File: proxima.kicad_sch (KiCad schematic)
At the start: 11 parts

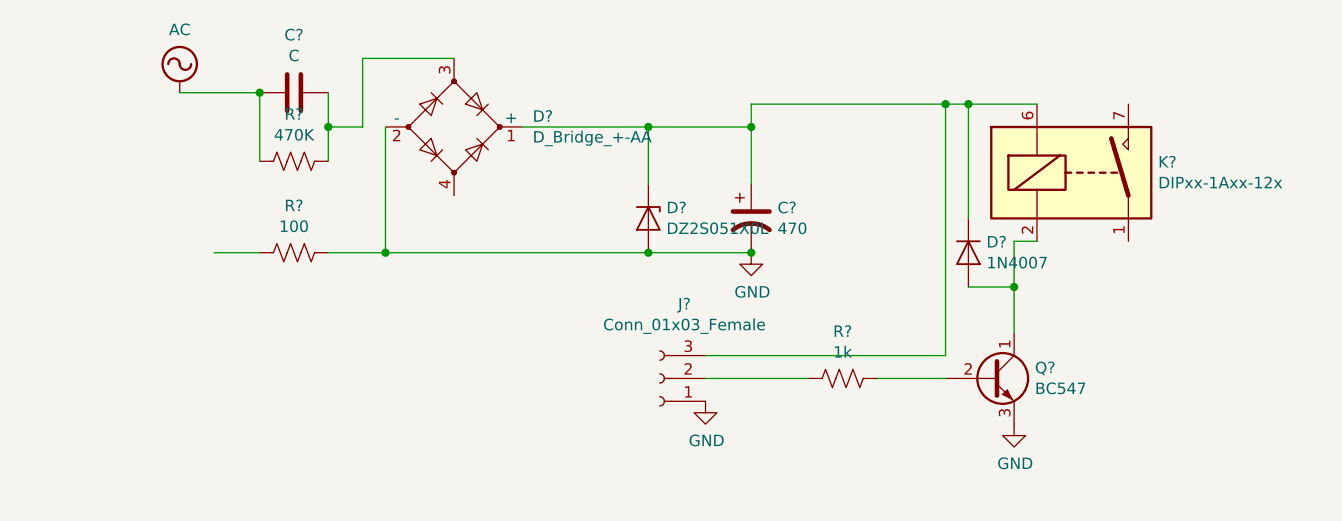
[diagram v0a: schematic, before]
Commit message: Annotate symbols
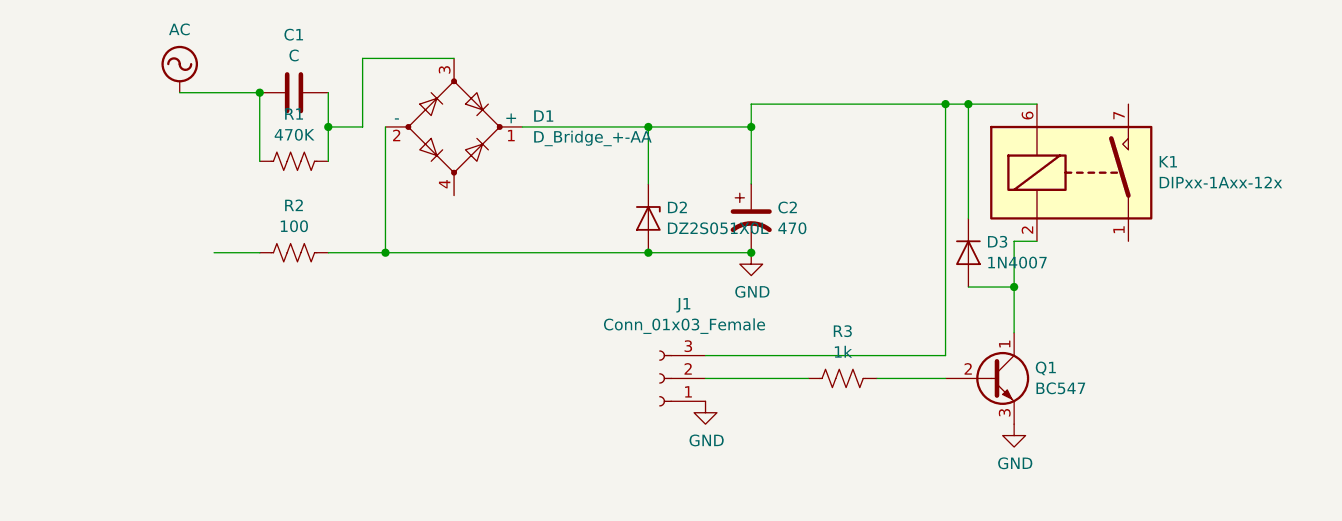
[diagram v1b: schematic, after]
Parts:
- gave numbers to parts that had none: 11
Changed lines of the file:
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@@
   (symbol (lib_id "proxima-rescue:C-Device") (at 124.46 77.47 270) (unit 1)
     (in_bom yes) (on_board yes)
-    (property "Reference" "C?" (id 0) (at 124.46 71.0692 90))
+    (property "Reference" "C1" (id 0) (at 124.46 71.0692 90))
     (property "Value" "C" (id 1) (at 124.46 73.3806 90))
     (property "Footprint" "" (id 2) (at 120.65 78.4352 0)
@@
   (symbol (lib_id "proxima-rescue:CP1-Device") (at 175.26 91.44 0) (unit 1)
     (in_bom yes) (on_board yes)
-    (property "Reference" "C?" (id 0) (at 178.181 90.2716 0)
+    (property "Reference" "C2" (id 0) (at 178.181 90.2716 0)
       (effects (font (size 1.27 1.27)) (justify left))
     )
@@
   (symbol (lib_id "proxima-rescue:D_Bridge_+-AA-Device") (at 142.24 81.28 0) (unit 1)
     (in_bom yes) (on_board yes)
-    (property "Reference" "D?" (id 0) (at 150.9776 80.1116 0)
+    (property "Reference" "D1" (id 0) (at 150.9776 80.1116 0)
       (effects (font (size 1.27 1.27)) (justify left))
     )
@@
   (symbol (lib_id "proxima-rescue:DZ2S051X0L-Diode") (at 163.83 91.44 270) (unit 1)
     (in_bom yes) (on_board yes)
-    (property "Reference" "D?" (id 0) (at 165.8366 90.2716 90)
+    (property "Reference" "D2" (id 0) (at 165.8366 90.2716 90)
       (effects (font (size 1.27 1.27)) (justify left))
     )
@@
   (symbol (lib_id "proxima-rescue:R_US-Device") (at 124.46 85.09 270) (unit 1)
     (in_bom yes) (on_board yes)
-    (property "Reference" "R?" (id 0) (at 124.46 79.883 90))
+    (property "Reference" "R1" (id 0) (at 124.46 79.883 90))
     (property "Value" "470K" (id 1) (at 124.46 82.1944 90))
     (property "Footprint" "" (id 2) (at 124.206 86.106 90)
@@
   (symbol (lib_id "proxima-rescue:R_US-Device") (at 124.46 95.25 270) (unit 1)
     (in_bom yes) (on_board yes)
-    (property "Reference" "R?" (id 0) (at 124.46 90.043 90))
+    (property "Reference" "R2" (id 0) (at 124.46 90.043 90))
     (property "Value" "100" (id 1) (at 124.46 92.3544 90))
     (property "Footprint" "" (id 2) (at 124.206 96.266 90)
@@
   (symbol (lib_id "proxima-rescue:AC-power") (at 111.76 77.47 0) (unit 1)
     (in_bom yes) (on_board yes)
-    (property "Reference" "#PWR?" (id 0) (at 111.76 80.01 0)
+    (property "Reference" "#PWR01" (id 0) (at 111.76 80.01 0)
       (effects (font (size 1.27 1.27)) hide)
     )
@@
   (symbol (lib_id "proxima-rescue:DIPxx-1Axx-12x-Relay") (at 212.09 86.36 0) (unit 1)
     (in_bom yes) (on_board yes)
-    (property "Reference" "K?" (id 0) (at 220.472 85.1916 0)
+    (property "Reference" "K1" (id 0) (at 220.472 85.1916 0)
       (effects (font (size 1.27 1.27)) (justify left))
     )
@@
   (symbol (lib_id "proxima-rescue:BC547-Transistor_BJT") (at 201.93 109.22 0) (unit 1)
     (in_bom yes) (on_board yes)
-    (property "Reference" "Q?" (id 0) (at 206.7814 108.0516 0)
+    (property "Reference" "Q1" (id 0) (at 206.7814 108.0516 0)
       (effects (font (size 1.27 1.27)) (justify left))
     )
@@
   (symbol (lib_id "proxima-rescue:Conn_01x03_Female-Connector") (at 165.1 109.22 180) (unit 1)
     (in_bom yes) (on_board yes)
-    (property "Reference" "J?" (id 0) (at 167.8432 100.965 0))
+    (property "Reference" "J1" (id 0) (at 167.8432 100.965 0))
     (property "Value" "Conn_01x03_Female" (id 1) (at 167.8432 103.2764 0))
     (property "Footprint" "" (id 2) (at 165.1 109.22 0)
@@
   (symbol (lib_id "proxima-rescue:R_US-Device") (at 185.42 109.22 270) (unit 1)
     (in_bom yes) (on_board yes)
-    (property "Reference" "R?" (id 0) (at 185.42 104.013 90))
+    (property "Reference" "R3" (id 0) (at 185.42 104.013 90))
     (property "Value" "1k" (id 1) (at 185.42 106.3244 90))
     (property "Footprint" "" (id 2) (at 185.166 110.236 90)
@@
   (symbol (lib_id "proxima-rescue:GND-power") (at 175.26 95.25 0) (unit 1)
     (in_bom yes) (on_board yes)
-    (property "Reference" "#PWR?" (id 0) (at 175.26 101.6 0)
+    (property "Reference" "#PWR03" (id 0) (at 175.26 101.6 0)
       (effects (font (size 1.27 1.27)) hide)
     )
@@
   (symbol (lib_id "proxima-rescue:GND-power") (at 204.47 114.3 0) (unit 1)
     (in_bom yes) (on_board yes)
-    (property "Reference" "#PWR?" (id 0) (at 204.47 120.65 0)
+    (property "Reference" "#PWR04" (id 0) (at 204.47 120.65 0)
       (effects (font (size 1.27 1.27)) hide)
     )
@@
   (symbol (lib_id "proxima-rescue:GND-power") (at 170.18 111.76 0) (unit 1)
     (in_bom yes) (on_board yes)
-    (property "Reference" "#PWR?" (id 0) (at 170.18 118.11 0)
+    (property "Reference" "#PWR02" (id 0) (at 170.18 118.11 0)
       (effects (font (size 1.27 1.27)) hide)
     )
@@
   (symbol (lib_id "proxima-rescue:1N4007-Diode") (at 199.39 95.25 270) (unit 1)
     (in_bom yes) (on_board yes)
-    (property "Reference" "D?" (id 0) (at 201.3966 94.0816 90)
+    (property "Reference" "D3" (id 0) (at 201.3966 94.0816 90)
       (effects (font (size 1.27 1.27)) (justify left))
     )
@@
   (symbol_instances
     (path "/00000000-0000-0000-0000-00006363069b"
-      (reference "#PWR?") (unit 1) (value "AC") (footprint "")
+      (reference "#PWR01") (unit 1) (value "AC") (footprint "")
+    )
+    (path "/00000000-0000-0000-0000-0000636b6e73"
+      (reference "#PWR02") (unit 1) (value "GND") (footprint "")
     )
     (path "/00000000-0000-0000-0000-0000636b5108"
-      (reference "#PWR?") (unit 1) (value "GND") (footprint "")
+      (reference "#PWR03") (unit 1) (value "GND") (footprint "")
     )
     (path "/00000000-0000-0000-0000-0000636b5b8d"
-      (reference "#PWR?") (unit 1) (value "GND") (footprint "")
-    )
-    (path "/00000000-0000-0000-0000-0000636b6e73"
-      (reference "#PWR?") (unit 1) (value "GND") (footprint "")
+      (reference "#PWR04") (unit 1) (value "GND") (footprint "")
     )
     (path "/00000000-0000-0000-0000-00006362c072"
-      (reference "C?") (unit 1) (value "C") (footprint "")
+      (reference "C1") (unit 1) (value "C") (footprint "")
     )
     (path "/00000000-0000-0000-0000-00006362c51f"
-      (reference "C?") (unit 1) (value "470") (footprint "")
+      (reference "C2") (unit 1) (value "470") (footprint "")
     )
     (path "/00000000-0000-0000-0000-00006362d2c4"
-      (reference "D?") (unit 1) (value "D_Bridge_+-AA") (footprint "")
+      (reference "D1") (unit 1) (value "D_Bridge_+-AA") (footprint "")
     )
     (path "/00000000-0000-0000-0000-00006362e947"
-      (reference "D?") (unit 1) (value "DZ2S051X0L") (footprint "Diode_SMD:D_SOD-523")
+      (reference "D2") (unit 1) (value "DZ2S051X0L") (footprint "Diode_SMD:D_SOD-523")
     )
     (path "/00000000-0000-0000-0000-0000636b8955"
-      (reference "D?") (unit 1) (value "1N4007") (footprint "Diode_THT:D_DO-41_SOD81_P10.16mm_Horizontal")
+      (reference "D3") (unit 1) (value "1N4007") (footprint "Diode_THT:D_DO-41_SOD81_P10.16mm_Horizontal")
     )
     (path "/00000000-0000-0000-0000-0000636a603e"
-      (reference "J?") (unit 1) (value "Conn_01x03_Female") (footprint "")
+      (reference "J1") (unit 1) (value "Conn_01x03_Female") (footprint "")
     )
     (path "/00000000-0000-0000-0000-000063693c13"
-      (reference "K?") (unit 1) (value "DIPxx-1Axx-12x") (footprint "Relay_THT:Relay_StandexMeder_DIP_LowProfile")
+      (reference "K1") (unit 1) (value "DIPxx-1Axx-12x") (footprint "Relay_THT:Relay_StandexMeder_DIP_LowProfile")
     )
     (path "/00000000-0000-0000-0000-000063695ded"
-      (reference "Q?") (unit 1) (value "BC547") (footprint "Package_TO_SOT_THT:TO-92_Inline")
+      (reference "Q1") (unit 1) (value "BC547") (footprint "Package_TO_SOT_THT:TO-92_Inline")
     )
     (path "/00000000-0000-0000-0000-00006362f5cb"
-      (reference "R?") (unit 1) (value "470K") (footprint "")
+      (reference "R1") (unit 1) (value "470K") (footprint "")
     )
     (path "/00000000-0000-0000-0000-000063630132"
-      (reference "R?") (unit 1) (value "100") (footprint "")
+      (reference "R2") (unit 1) (value "100") (footprint "")
     )
     (path "/00000000-0000-0000-0000-0000636acf39"
-      (reference "R?") (unit 1) (value "1k") (footprint "")
-    )
-  )
+      (reference "R3") (unit 1) (value "1k") (footprint "")
+    )
+  )

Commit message: Substitute proxima-rescue lib
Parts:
- C1: symbol proxima-rescue:C-Device -> Device:C
- C2: symbol proxima-rescue:CP1-Device -> Device:C_Polarized_US
- D1: symbol proxima-rescue:D_Bridge_+-AA-Device -> Device:D_Bridge_+AA-
- D2: symbol proxima-rescue:DZ2S051X0L-Diode -> Diode:DZ2S051X0L
- D3: symbol proxima-rescue:1N4007-Diode -> Diode:1N4007
- J1: symbol proxima-rescue:Conn_01x03_Female-Connector -> Connector:Conn_01x03_Female
- K1: symbol proxima-rescue:DIPxx-1Axx-12x-Relay -> Relay:DIPxx-1Axx-12x
- Q1: symbol proxima-rescue:BC547-Transistor_BJT -> Transistor_BJT:BC547
- R1, R2, R3: symbol proxima-rescue:R_US-Device -> Device:R_US
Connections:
- net GND: now also D1.4 (-); no longer D1.2 (-)
- net at C1.1, R1.1: now also D1.2; no longer D1.3
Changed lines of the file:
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@@
     (stroke (width 0) (type default) (color 0 0 0 0))
   )
-  (symbol (lib_id "proxima-rescue:C-Device") (at 124.46 77.47 270) (unit 1)
+  (symbol (lib_id "Device:C") (at 124.46 77.47 270) (unit 1)
     (in_bom yes) (on_board yes)
     (property "Reference" "C1" (id 0) (at 124.46 71.0692 90))
@@
     (pin "2")
   )
-  (symbol (lib_id "proxima-rescue:CP1-Device") (at 175.26 91.44 0) (unit 1)
+  (symbol (lib_id "Device:C_Polarized_US") (at 175.26 91.44 0) (unit 1)
     (in_bom yes) (on_board yes)
     (property "Reference" "C2" (id 0) (at 178.181 90.2716 0)
@@
     (pin "2")
   )
-  (symbol (lib_id "proxima-rescue:D_Bridge_+-AA-Device") (at 142.24 81.28 0) (unit 1)
+  (symbol (lib_id "Device:D_Bridge_+AA-") (at 142.24 81.28 0) (unit 1)
     (in_bom yes) (on_board yes)
     (property "Reference" "D1" (id 0) (at 150.9776 80.1116 0)
@@
     (pin "4")
   )
-  (symbol (lib_id "proxima-rescue:DZ2S051X0L-Diode") (at 163.83 91.44 270) (unit 1)
+  (symbol (lib_id "Diode:DZ2S051X0L") (at 163.83 91.44 270) (unit 1)
     (in_bom yes) (on_board yes)
     (property "Reference" "D2" (id 0) (at 165.8366 90.2716 90)
@@
     (pin "2")
   )
-  (symbol (lib_id "proxima-rescue:R_US-Device") (at 124.46 85.09 270) (unit 1)
+  (symbol (lib_id "Device:R_US") (at 124.46 85.09 270) (unit 1)
     (in_bom yes) (on_board yes)
     (property "Reference" "R1" (id 0) (at 124.46 79.883 90))
@@
     (pin "2")
   )
-  (symbol (lib_id "proxima-rescue:R_US-Device") (at 124.46 95.25 270) (unit 1)
+  (symbol (lib_id "Device:R_US") (at 124.46 95.25 270) (unit 1)
     (in_bom yes) (on_board yes)
     (property "Reference" "R2" (id 0) (at 124.46 90.043 90))
@@
     (pin "2")
   )
-  (symbol (lib_id "proxima-rescue:AC-power") (at 111.76 77.47 0) (unit 1)
+  (symbol (lib_id "power:AC") (at 111.76 77.47 0) (unit 1)
     (in_bom yes) (on_board yes)
     (property "Reference" "#PWR01" (id 0) (at 111.76 80.01 0)
@@
     (pin "1")
   )
-  (symbol (lib_id "proxima-rescue:DIPxx-1Axx-12x-Relay") (at 212.09 86.36 0) (unit 1)
+  (symbol (lib_id "Relay:DIPxx-1Axx-12x") (at 212.09 86.36 0) (unit 1)
     (in_bom yes) (on_board yes)
     (property "Reference" "K1" (id 0) (at 220.472 85.1916 0)
@@
     (pin "8")
   )
-  (symbol (lib_id "proxima-rescue:BC547-Transistor_BJT") (at 201.93 109.22 0) (unit 1)
+  (symbol (lib_id "Transistor_BJT:BC547") (at 201.93 109.22 0) (unit 1)
     (in_bom yes) (on_board yes)
     (property "Reference" "Q1" (id 0) (at 206.7814 108.0516 0)
@@
       (effects (font (size 1.27 1.27) italic) (justify left) hide)
     )
-    (property "Datasheet" "http://www.fairchildsemi.com/ds/BC/BC547.pdf" (id 3) (at 201.93 109.22 0)
+    (property "Datasheet" "https://www.onsemi.com/pub/Collateral/BC550-D.pdf" (id 3) (at 201.93 109.22 0)
       (effects (font (size 1.27 1.27)) (justify left) hide)
     )
@@
     (pin "3")
   )
-  (symbol (lib_id "proxima-rescue:Conn_01x03_Female-Connector") (at 165.1 109.22 180) (unit 1)
+  (symbol (lib_id "Connector:Conn_01x03_Female") (at 165.1 109.22 180) (unit 1)
     (in_bom yes) (on_board yes)
     (property "Reference" "J1" (id 0) (at 167.8432 100.965 0))
@@
     (pin "3")
   )
-  (symbol (lib_id "proxima-rescue:R_US-Device") (at 185.42 109.22 270) (unit 1)
+  (symbol (lib_id "Device:R_US") (at 185.42 109.22 270) (unit 1)
     (in_bom yes) (on_board yes)
     (property "Reference" "R3" (id 0) (at 185.42 104.013 90))
@@
     (pin "1")
   )
-  (symbol (lib_id "proxima-rescue:1N4007-Diode") (at 199.39 95.25 270) (unit 1)
+  (symbol (lib_id "Diode:1N4007") (at 199.39 95.25 270) (unit 1)
     (in_bom yes) (on_board yes)
     (property "Reference" "D3" (id 0) (at 201.3966 94.0816 90)

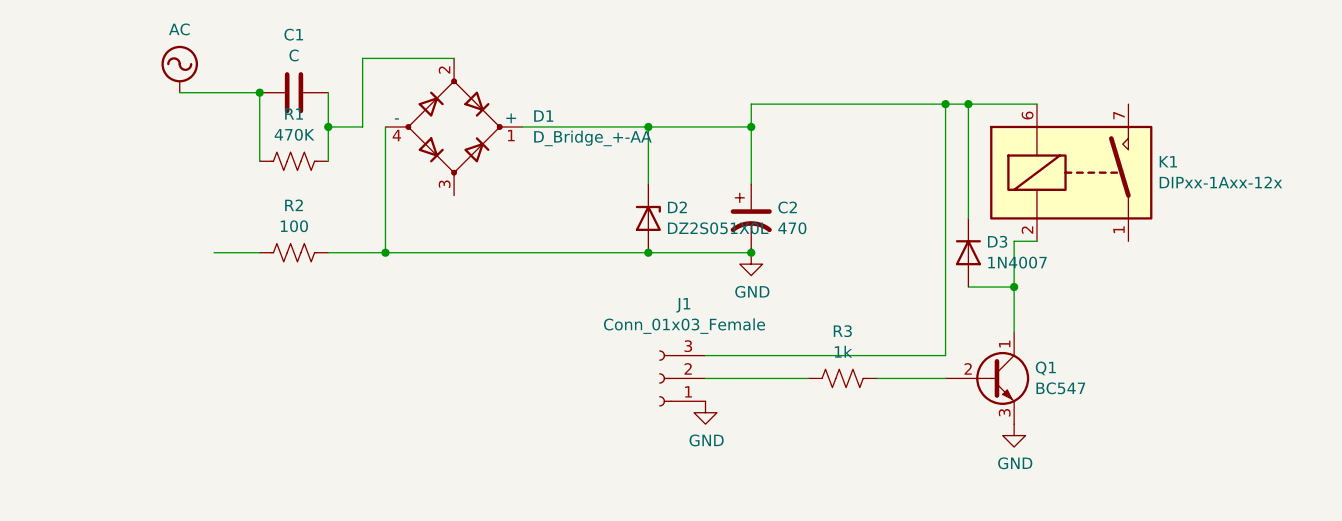
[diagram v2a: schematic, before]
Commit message: Initial ERC Fixed wheatstone bridge error Added screw terminal A.C input Added PWR_FLAGs
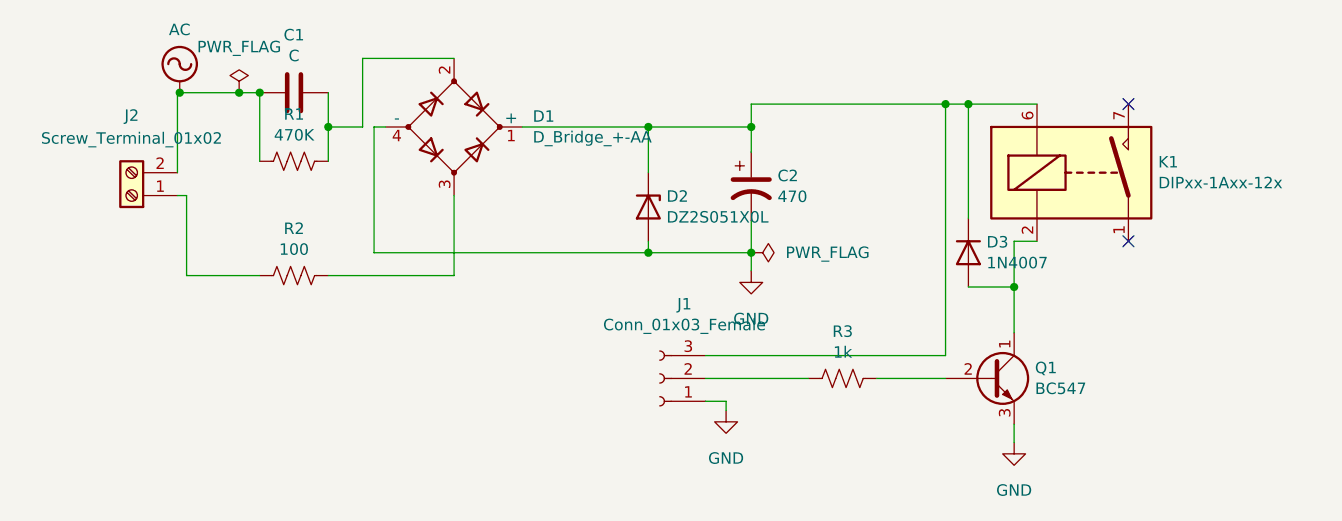
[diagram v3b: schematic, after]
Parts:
- added J2: Screw_Terminal_01x02, symbol Connector:Screw_Terminal_01x02
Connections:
- net AC: now also J2.2 (Pin_2)
- net GND: no longer R2.1
- net at D1.3: now also R2.1
- net at R2.2: now also J2.1 (Pin_1)
- no-connect marks 0 -> 2
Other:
- company: (none) -> ZanjTech Society
- title: (none) -> Proxima
- moved on the sheet: C2, D2, R2

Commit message: Some symbol values
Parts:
- C1: value C -> 1u/400V
- C2: value 470 -> 470nF
- D2: value DZ2S051X0L -> 12v/1w
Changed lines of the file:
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@@
     (in_bom yes) (on_board yes)
     (property "Reference" "C1" (id 0) (at 124.46 71.0692 90))
-    (property "Value" "C" (id 1) (at 124.46 73.3806 90))
+    (property "Value" "1u/400V" (id 1) (at 124.46 73.3806 90))
     (property "Footprint" "" (id 2) (at 120.65 78.4352 0)
       (effects (font (size 1.27 1.27)) hide)
@@
       (effects (font (size 1.27 1.27)) (justify left))
     )
-    (property "Value" "470" (id 1) (at 178.181 89.027 0)
+    (property "Value" "470nF" (id 1) (at 178.181 89.027 0)
       (effects (font (size 1.27 1.27)) (justify left))
     )
@@
       (effects (font (size 1.27 1.27)) (justify left))
     )
-    (property "Value" "DZ2S051X0L" (id 1) (at 165.8366 91.313 90)
+    (property "Value" "12v/1w" (id 1) (at 165.8366 91.313 90)
       (effects (font (size 1.27 1.27)) (justify left))
     )
@@
     )
     (path "/00000000-0000-0000-0000-00006362c072"
-      (reference "C1") (unit 1) (value "C") (footprint "")
+      (reference "C1") (unit 1) (value "1u/400V") (footprint "")
     )
     (path "/00000000-0000-0000-0000-00006362c51f"
-      (reference "C2") (unit 1) (value "470") (footprint "")
+      (reference "C2") (unit 1) (value "470nF") (footprint "")
     )
     (path "/00000000-0000-0000-0000-00006362d2c4"
@@
     )
     (path "/00000000-0000-0000-0000-00006362e947"
-      (reference "D2") (unit 1) (value "DZ2S051X0L") (footprint "Diode_SMD:D_SOD-523")
+      (reference "D2") (unit 1) (value "12v/1w") (footprint "Diode_SMD:D_SOD-523")
     )
     (path "/00000000-0000-0000-0000-0000636b8955"
